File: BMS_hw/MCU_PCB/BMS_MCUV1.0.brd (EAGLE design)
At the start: 60 x 30 mm, 42 parts, among them IC2 SST25VF020B804ISA, Q1 CRYSTALS-GND-LID-IQXC-42

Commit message: @dsdwsw
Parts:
- removed R10: 10, ipc-7351-resistor:RESC1005X40AN
- removed R8: 2.2k, ipc-7351-resistor:RESC1005X40AN
- removed R9: 220, ipc-7351-resistor:RESC1005X40AN
- removed TP1, TP2: TP-SMD60, simpa:TP-SMD60
- R11, R12: value 100 -> 100R
- moved R11 23.3 mm to (31.8, 8.89)
- moved R14 20.7 mm to (33.7, 10.2), turned to 0 degrees
- moved R12 20.4 mm to (33.7, 8.89), turned to 180 degrees
- moved R13 19.9 mm to (31.8, 10.2), turned to 180 degrees
- moved C12 5.43 mm to (27.9, 21.0), turned to 180 degrees
- moved C20 2.84 mm to (19.7, 6.35)
- moved L2 2.01 mm to (10.2, 5.08)
- moved R3 2.01 mm to (45.7, 18.4), turned to 0 degrees
- moved C11 1.52 mm to (23.5, 13.1), turned to 270 degrees
- moved C18 1.37 mm to (20.4, 12.1)
- moved IC2 1.27 mm to (5.08, 24.8)
- moved R7 0.92 mm to (43.4, 15.9), turned to 0 degrees
- moved C8 0.90 mm to (43.2, 13.3)
- moved C2 0.90 mm to (20.3, 22.2), turned to 135 degrees
- moved C19 0.68 mm to (21.2, 10.2)
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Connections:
- net N$42 renamed CS
- removed net C_FET: MCU2.14
- removed net DBG_TX: MCU2.12
- removed net D_FET: MCU2.1
- removed net FAULT: MCU2.13
- removed net ICSPCLK: MCU2.24
- removed net ICSPDAT: MCU2.11
- removed net INTL_IN2: MCU2.46
- removed net ISP: MCU2.33
- removed net N$10: MCU2.54
- removed net N$12: JP2.10, R10.2
- removed net N$13: JP2.9, R11.2
- removed net N$15: JP2.8, R12.2
- removed net N$16: MCU2.47, TP2.P$1
- removed net N$29: MCU2.27
- removed net N$30: MCU2.28
- removed net N$4: JP2.12, R8.2
- removed net N$40: MCU2.29
- removed net N$41: MCU2.30
- removed net N$43: MCU2.59
- removed net N$45: MCU2.5
- removed net N$46: MCU2.6
- removed net N$47: MCU2.8
- removed net N$5: MCU2.48, TP1.P$1
- removed net N$66: MCU2.60
- removed net N$67: MCU2.61
- removed net N$70: MCU2.3
- removed net N$71: MCU2.21
- removed net N$72: MCU2.22
- removed net N$74: MCU2.50
- removed net N$75: MCU2.51
- removed net N$77: MCU2.55
- removed net N$78: MCU2.45
- removed net N$79: MCU2.36
- removed net N$8: JP2.11, R9.2
- removed net N$80: MCU2.37
- removed net N$81: MCU2.2
- removed net N$9: MCU2.53
- removed net PCHG_FET: MCU2.31
- removed net RX: R8.1
- removed net SCL: R12.1, R14.2
- removed net SDA: R11.1, R13.2
- removed net TX: R9.1
- new net !OLED_SCL: JP1.5, R12.2
- new net !OLED_SDA: JP1.6, R11.2
- new net CSB: JP1.4, MCU2.18
- new net MISO: JP1.3, MCU2.17
- new net MOSI: JP1.1, MCU2.15
- new net OLED_SCL: MCU2.21, R12.1, R14.2
- new net OLED_SDA: MCU2.22, R11.1, R13.2
- new net PGEC2: JP2.12, MCU2.44
- new net PGED2: JP2.11, MCU2.43
- new net RX_1: JP2.9, MCU2.1
- new net RX_2: JP2.8, MCU2.2
- new net S-LED_1: JP5.1, MCU2.49
- new net S-LED_2: JP5.2, MCU2.50
- new net S-LED_3: JP5.3, MCU2.51
- new net S-LED_4: JP5.4, MCU2.52
- new net S-LED_5: JP5.5, MCU2.53
- new net S-LED_6: JP5.6, MCU2.54
- new net SCLK: JP1.2, MCU2.16
- new net TX_1: JP2.7, MCU2.3
- new net TX_2: JP2.6, MCU2.5
- net !MCLR: now also JP2.10
- net 3.3V: now also JP5.7
- net CAN_RX: now also MCU2.31; no longer MCU2.15
- net CAN_TX: now also MCU2.30; no longer MCU2.16
- net SCK: now also MCU2.60; no longer MCU2.49
- net SI: now also MCU2.59; no longer MCU2.52
- net SO: now also MCU2.61; no longer MCU2.63
- net VDD: no longer R10.1
- net WP#: no longer MCU2.62
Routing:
- net PGEC2: track 0.00 -> 43.4 mm
- net PGED2: track 0.00 -> 42.3 mm
- net VDD: track 87.6 -> 60.5 mm
- net OLED_SCL: track 0.00 -> 26.2 mm, vias 0 -> 2
- net S-LED_6: track 0.00 -> 23.0 mm, vias 0 -> 1
- net S-LED_5: track 0.00 -> 20.2 mm, vias 0 -> 1
- net OLED_SDA: track 0.00 -> 19.5 mm, vias 0 -> 2
- net S-LED_4: track 0.00 -> 17.0 mm, vias 0 -> 1
- net !OLED_SCL: track 0.00 -> 15.3 mm, vias 0 -> 2
- net S-LED_3: track 0.00 -> 14.4 mm, vias 0 -> 1
- net SCL: track 11.4 -> 0.00 mm
- net !OLED_SDA: track 0.00 -> 11.2 mm
- net S-LED_2: track 0.00 -> 10.3 mm
- net CSB: track 0.00 -> 10.0 mm
- net CAN_TX: track 19.7 -> 10.4 mm, vias 2 -> 0
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
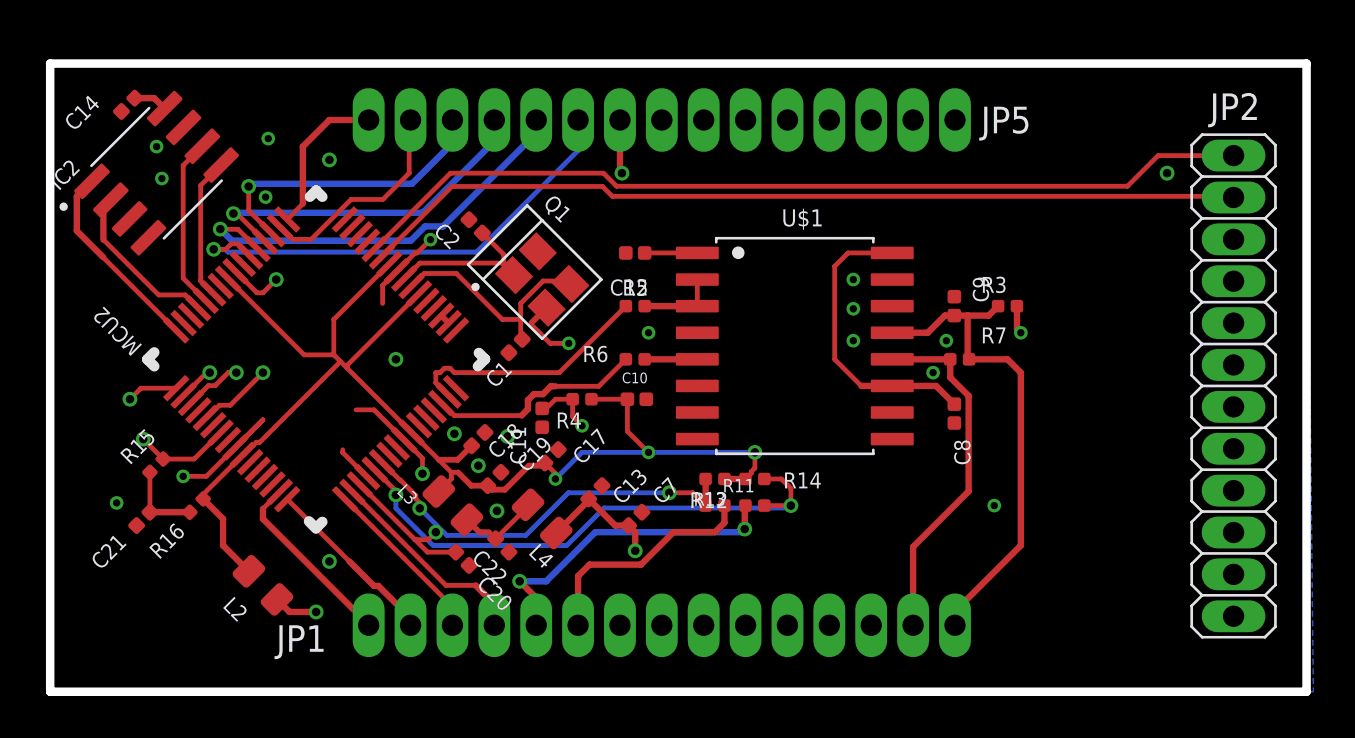
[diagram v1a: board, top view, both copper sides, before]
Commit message: afe mcu schematic updated
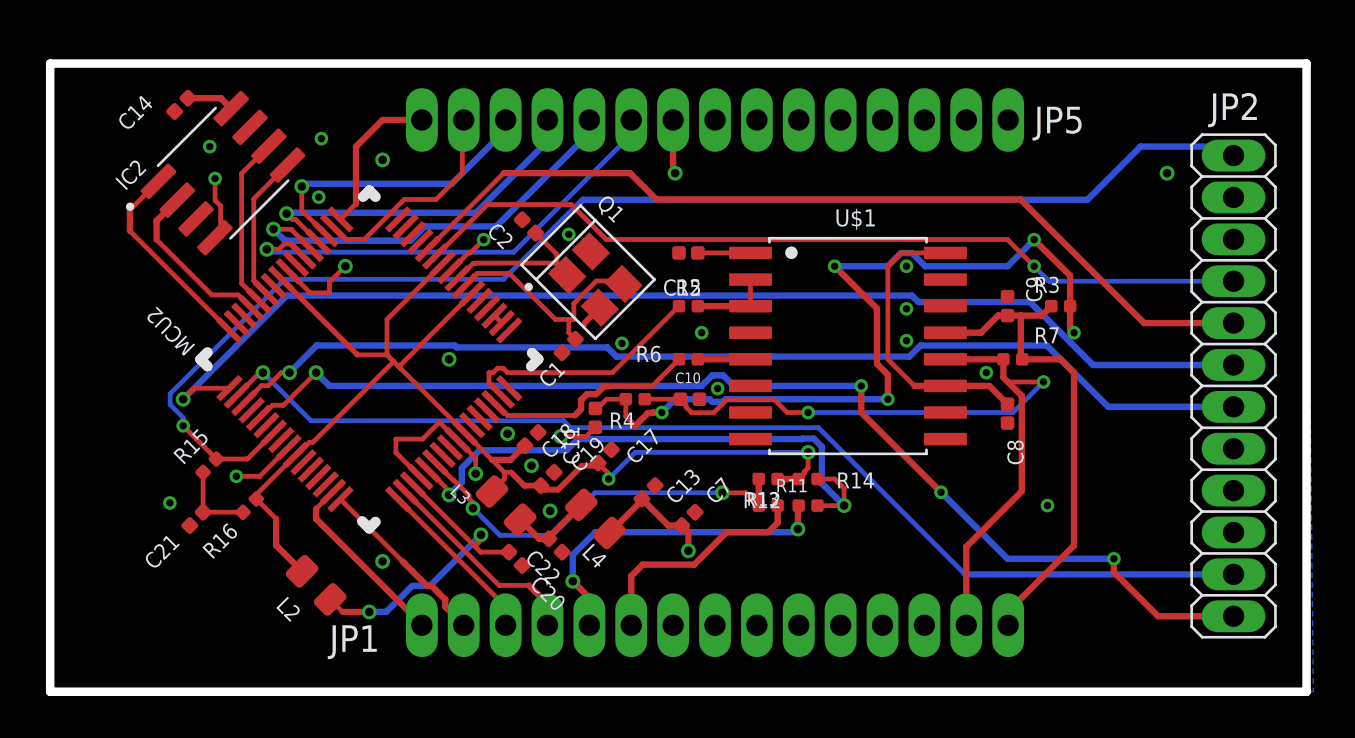
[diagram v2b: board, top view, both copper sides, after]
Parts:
- moved IC2 3.18 mm to (8.26, 24.8)
- moved C20 2.54 mm to (22.2, 6.35)
- moved R4 2.54 mm to (27.9, 14.0)
- moved MCU2 2.54 mm to (15.2, 15.9)
- moved C14 2.54 mm to (6.26, 28.0)
- moved C21 2.54 mm to (6.99, 8.26)
- moved R15 2.54 mm to (7.62, 10.8)
- moved R16 2.54 mm to (9.53, 8.89)
- moved C1 2.54 mm to (24.8, 16.5)
- moved C10 2.54 mm to (30.6, 14.0)
- moved C11 2.54 mm to (26.0, 13.1)
- moved C12 2.54 mm to (30.5, 21.0)
- moved C13 2.54 mm to (28.6, 9.53)
- moved C17 2.54 mm to (26.5, 11.2)
- moved C18 2.54 mm to (23.0, 12.1)
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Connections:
- net !MCLR: now also JP2.12; no longer JP2.10
- net 3.3V: now also JP2.11
- net GND: now also JP2.10, JP2.3, JP2.4, JP2.5
- net PGEC2: now also JP2.8; no longer JP2.12
- net PGED2: now also JP2.9; no longer JP2.11
- net RX_1: now also JP2.7; no longer JP2.9
- net RX_2: now also JP2.2; no longer JP2.8
- net TX_1: now also JP2.6; no longer JP2.7
- net TX_2: now also JP2.1; no longer JP2.6
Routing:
- net !MCLR: track 4.61 -> 63.2 mm
- net RX_1: track 2.43 -> 56.0 mm
- net RX_2: track 1.70 -> 52.0 mm
- net TX_2: track 4.12 -> 53.8 mm, vias 1 -> 4
- net TX_1: track 2.77 -> 50.0 mm
- net N$11: track 27.2 -> 39.0 mm, vias 2 -> 5
- net VDD: track 60.5 -> 67.5 mm
- net OLED_SCL: track 26.2 -> 27.9 mm
- net PGED2: track 42.3 -> 40.7 mm, vias 0 -> 1
- net CANL: track 38.1 -> 39.4 mm, vias 1 -> 2
- net N$32: track 16.5 -> 15.6 mm
- net !OLED_SCL: track 15.3 -> 16.1 mm
- net N$14: track 1.64 -> 2.27 mm
- net GND: track 23.4 -> 23.2 mm, vias 25 -> 26

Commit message: afe ver 1.1 added@itt@20
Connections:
- new net CHG_GATE: JP5.9, MCU2.29
- new net DSG_GATE: JP5.8, MCU2.32
- new net FLOUT: JP1.7, MCU2.12
- new net KEY-IN: JP1.13, MCU2.13
- new net PCHG_GATE: JP5.10, MCU2.28
- new net RDD: JP5.12
- new net SGNL1: JP5.11
- net 3.3V: now also JP5.13
- net 5V: now also JP1.10, JP1.11
- net GND: now also JP1.12, JP1.8, JP1.9, JP5.14, JP5.15
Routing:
- net KEY-IN: track 0.00 -> 43.5 mm, vias 0 -> 3
- net 3.3V: track 8.61 -> 38.4 mm
- net FLOUT: track 0.00 -> 26.5 mm, vias 0 -> 1
- net PCHG_GATE: track 0.00 -> 25.2 mm, vias 0 -> 1
- net CHG_GATE: track 0.00 -> 22.6 mm, vias 0 -> 1
- net DSG_GATE: track 0.00 -> 18.2 mm, vias 0 -> 1
- net 5V: track 14.1 -> 31.3 mm
- net N$4: track 2.27 -> 0.00 mm
- net GND: vias 26 -> 27

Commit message: itt@21
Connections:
- net 3.3V: now also JP2.2; no longer JP2.11
- net GND: now also JP2.1, JP2.6, JP2.9; no longer JP2.10, JP2.4, JP2.5
- net PGEC2: now also JP2.10; no longer JP2.8
- net PGED2: now also JP2.11; no longer JP2.9
- net RX_1: now also JP2.8; no longer JP2.7
- net RX_2: now also JP2.5; no longer JP2.2
- net TX_1: now also JP2.7; no longer JP2.6
- net TX_2: now also JP2.4; no longer JP2.1
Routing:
- net 3.3V: track 38.4 -> 54.1 mm, vias 2 -> 4
- net S-LED_2: track 10.3 -> 14.0 mm
- net TX_2: track 53.8 -> 51.0 mm, vias 4 -> 3
- net RX_2: track 52.0 -> 49.8 mm
- net N$4: track 0.00 -> 2.27 mm
- net PGEC2: track 42.9 -> 41.3 mm
- net PGED2: track 40.7 -> 41.7 mm
- net TX_1: track 50.0 -> 49.2 mm
- net RX_1: track 56.0 -> 55.2 mm
- net N$11: track 39.0 -> 39.7 mm
- net PCHG_GATE: track 25.2 -> 24.7 mm
- net GND: vias 27 -> 40

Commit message: replace part with fod8384 with tlp152 added datasheet in doc folder
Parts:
- removed C7: (no value), ipc-7351-capacitor:CAPC1005X60N
- C13: value (none) -> 10uF
- R5, R6: value (none) -> 0E
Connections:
- net 3.3V: now also C12.1, U$1.1; no longer C7.1
- net GND: no longer C7.2
- net N$3: now also R5.2, U$1.3; no longer C12.1, U$1.1
- net N$7: no longer R5.2, U$1.3
- net RDD: now also MCU2.33
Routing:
- net N$7: track 3.79 -> 0.00 mm
- net N$3: track 2.52 -> 0.00 mm
- net 3.3V: track 54.1 -> 54.7 mm, vias 4 -> 3

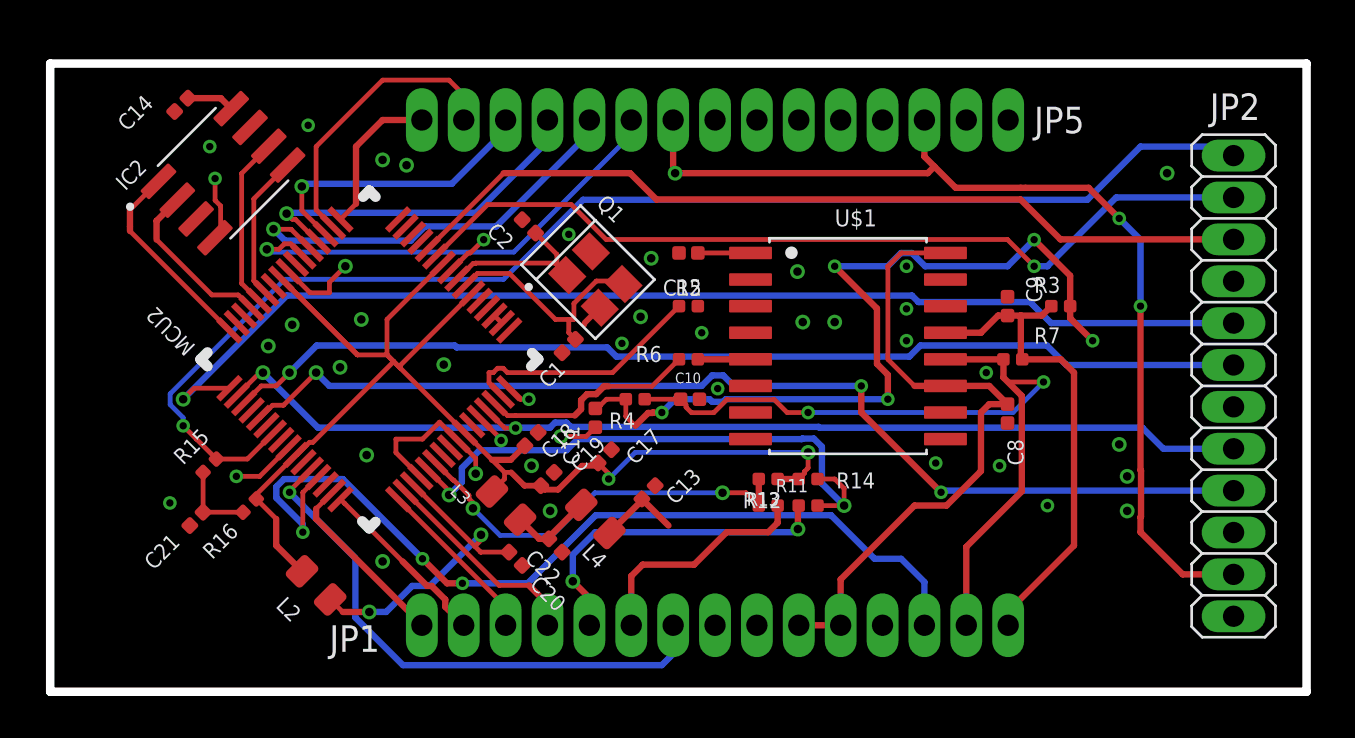
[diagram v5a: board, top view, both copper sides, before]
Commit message: afe and piggy board bom layout and schematic all changed for final only dc-dc convertor replacement required !
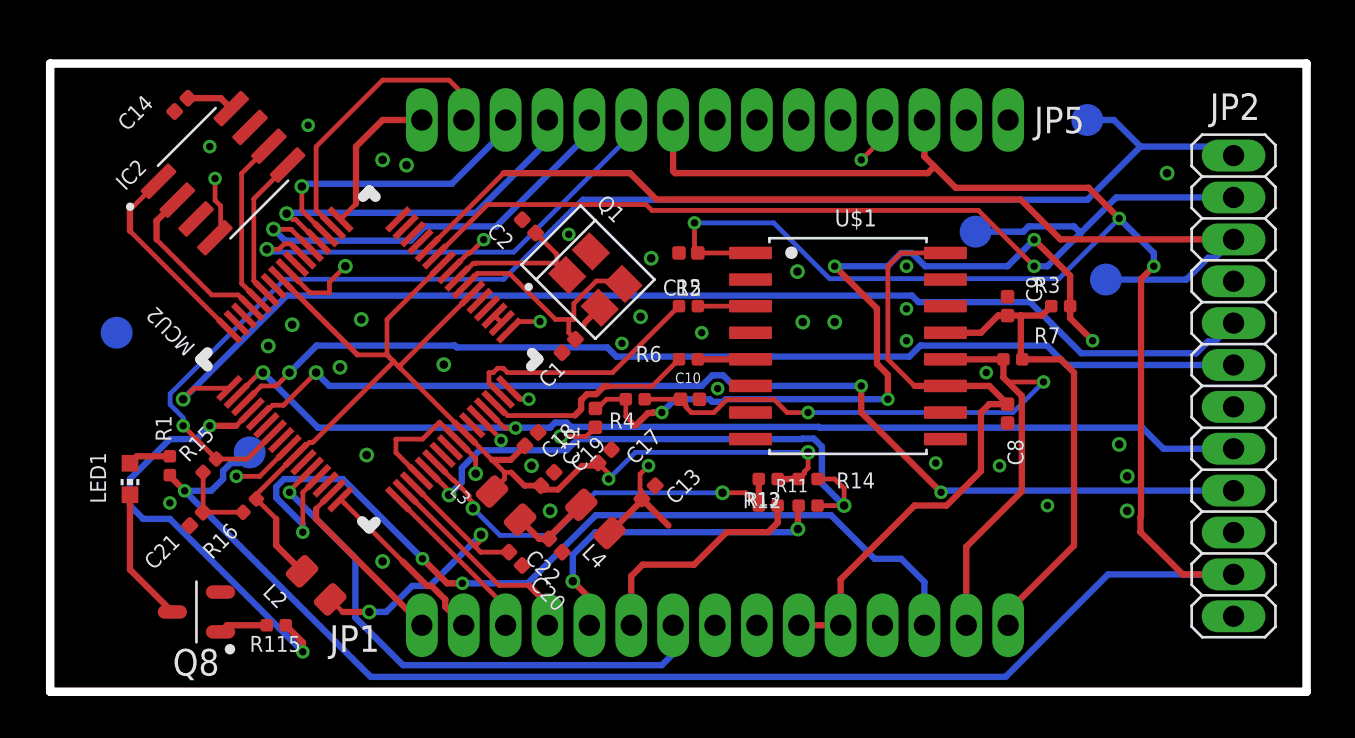
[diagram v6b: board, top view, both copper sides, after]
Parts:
- added LED1: (no value), adafruit:CHIP-LED0603
- added Q8: (no value), ipc-7351-transistor:SOT95P280X135-3N
- added R1, R115: 330E, ipc-7351-resistor:RESC1005X40AN
- added TP1, TP2, TP3, TP4, TP5: TP-SMD60, simpa:TP-SMD60
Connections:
- removed net N$44: MCU2.4
- removed net N$73: MCU2.23
- new net IND_LED: MCU2.4, R115.2
- new net N$5: LED1.A, R1.2
- new net N$8: LED1.C, Q8.3
- net !MCLR: now also TP5.P$1
- net 3.3V: now also R1.1, TP3.P$1
- net GND: now also Q8.2, TP4.P$1, U$1.2
- net N$7: now also Q8.1, R115.1; no longer U$1.2
- net PGEC2: now also TP2.P$1
- net PGED2: now also TP1.P$1
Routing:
- net 3.3V: track 54.7 -> 142.0 mm, vias 3 -> 5
- net RDD: track 0.00 -> 35.5 mm, vias 0 -> 2
- net IND_LED: track 0.00 -> 21.2 mm, vias 0 -> 2
- net PGEC2: track 41.3 -> 48.2 mm
- net N$8: track 0.00 -> 6.44 mm
- net PGED2: track 41.7 -> 47.0 mm
- net !MCLR: track 63.2 -> 66.2 mm
- net N$3: track 0.00 -> 2.52 mm
- net N$7: track 0.00 -> 2.34 mm
- net N$5: track 0.00 -> 2.04 mm
- net RX_1: track 55.2 -> 56.4 mm

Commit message: afe and piggy sch layout itt!
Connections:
- removed net N$4: C14.1, IC2.8
- net 3.3V: now also C14.1, IC2.8
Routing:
- net 3.3V: track 142.0 -> 147.3 mm, vias 5 -> 6
- net N$4: track 2.27 -> 0.00 mm
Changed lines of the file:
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@@
 <drawing>
 <settings>
-<setting alwaysvectorfont="yes"/>
+<setting alwaysvectorfont="no"/>
 <setting verticaltext="up"/>
 </settings>
@@
 <layers>
 <layer number="1" name="Top" color="4" fill="1" visible="yes" active="yes"/>
-<layer number="2" name="Route2" color="16" fill="1" visible="no" active="yes"/>
+<layer number="2" name="Route2" color="16" fill="1" visible="yes" active="yes"/>
 <layer number="3" name="Route3" color="17" fill="1" visible="no" active="no"/>
 <layer number="4" name="Route4" color="18" fill="1" visible="no" active="no"/>
@@
 <layer number="13" name="Route13" color="21" fill="1" visible="no" active="no"/>
 <layer number="14" name="Route14" color="22" fill="1" visible="no" active="no"/>
-<layer number="15" name="Route15" color="23" fill="1" visible="no" active="yes"/>
+<layer number="15" name="Route15" color="23" fill="1" visible="yes" active="yes"/>
 <layer number="16" name="Bottom" color="1" fill="1" visible="yes" active="yes"/>
 <layer number="17" name="Pads" color="2" fill="1" visible="yes" active="yes"/>
@@
 <wire x1="8.62813125" y1="10.9192" x2="9.0142" y2="10.9192" width="0.3048" layer="16"/>
 <wire x1="9.0142" y1="10.9192" x2="9.525" y2="11.43" width="0.3048" layer="16"/>
+<contactref element="IC2" pad="8"/>
+<contactref element="C14" pad="1"/>
+<wire x1="6.57839375" y1="28.347996875" x2="8.14389375" y2="28.347996875" width="0.3048" layer="1"/>
+<wire x1="8.14389375" y1="28.347996875" x2="8.64390625" y2="27.847984375" width="0.3048" layer="1"/>
+<wire x1="8.64390625" y1="27.847984375" x2="9.370921875" y2="28.575" width="0.3048" layer="1"/>
+<wire x1="9.370921875" y1="28.575" x2="11.43" y2="28.575" width="0.3048" layer="1"/>
+<via x="11.43" y="28.575" extent="1-15" drill="0.35"/>
 </signal>
 <signal name="N$6">
@@
 <wire x1="29.75" y1="1.81" x2="29.75" y2="3.175" width="0.3048" layer="16"/>
 </signal>
-<signal name="N$4">
-<contactref element="IC2" pad="8"/>
-<contactref element="C14" pad="1"/>
-<wire x1="6.57839375" y1="28.347996875" x2="8.14389375" y2="28.347996875" width="0.3048" layer="1"/>
-<wire x1="8.14389375" y1="28.347996875" x2="8.64390625" y2="27.847984375" width="0.3048" layer="1"/>
-</signal>
 <signal name="N$3">
